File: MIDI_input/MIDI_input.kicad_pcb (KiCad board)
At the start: 2 copper layers, 50 x 40 mm, 21 parts, among them J1 Conn_01x04, U1 6N138

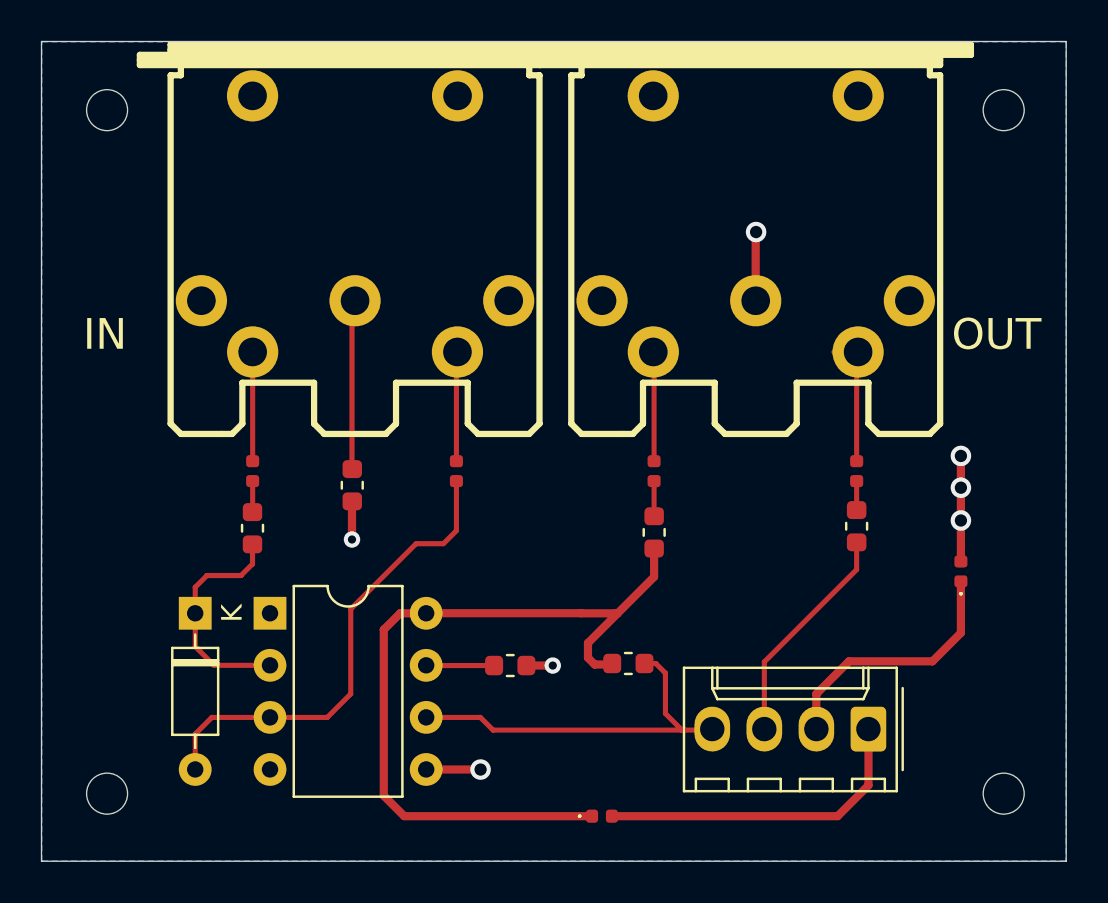
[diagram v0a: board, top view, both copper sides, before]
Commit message: Updates MIDI IO board
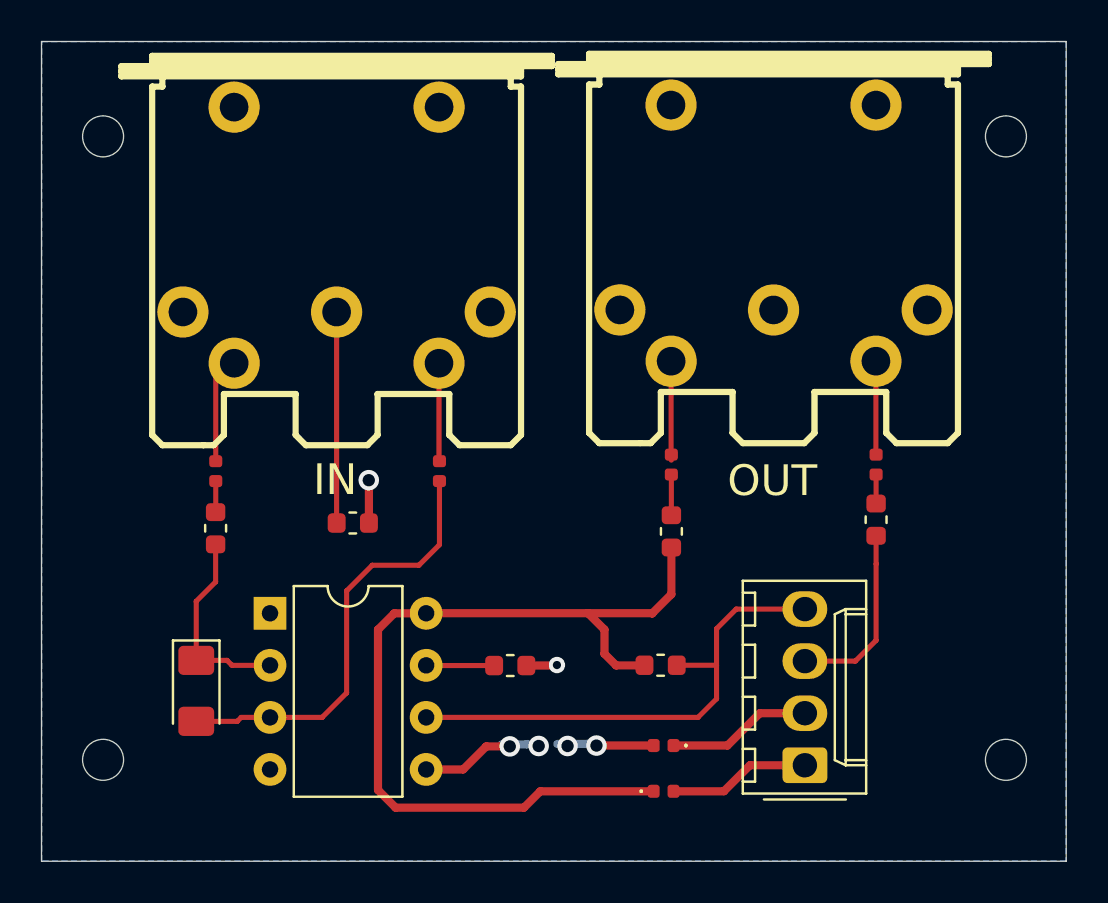
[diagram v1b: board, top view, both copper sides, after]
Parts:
- D1: footprint Diode_THT:D_DO-35_SOD27_P7.62mm_Horizontal -> Diode_SMD:D_1206_3216Metric_Pad1.42x1.75mm_HandSolder
- moved D3 16.8 mm to (44.3, 48.4), turned to 180 degrees
- moved D1 3.79 mm to (21.5, 45.8)
- moved J1 3.57 mm to (51.2, 49.4), turned to 90 degrees
- moved D2 3.24 mm to (44.3, 50.6)
- moved C1 1.84 mm to (29.2, 37.6), turned to 0 degrees
- moved FB3 1.80 mm to (22.5, 35.0)
- moved R3 1.80 mm to (22.5, 37.8)
- moved H2 1.66 mm to (17.0, 49.1)
- moved H4 1.65 mm to (61.0, 49.1)
- moved R4 1.58 mm to (44.2, 44.5)
- moved H1 1.29 mm to (17.0, 18.7)
- moved H3 1.28 mm to (61.0, 18.7)
- moved J_IN_1 1.06 mm to (28.4, 24.3)
- moved FB1 1.00 mm to (54.7, 34.7)
- moved R1 1.00 mm to (54.7, 37.4)
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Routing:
- net Net-(D2-Pad2): track 15.9 -> 6.94 mm
- net RX: track 18.6 -> 24.6 mm
- net +5V: track 37.7 -> 43.4 mm
- net Net-(D3-Pad1): track 12.5 -> 7.06 mm
- net Net-(C1-Pad1): track 8.14 -> 10.3 mm
- net TX: track 11.0 -> 9.00 mm
- net Net-(D1-Pad2): track 23.3 -> 21.5 mm
- net Net-(D1-Pad1): track 11.1 -> 9.75 mm
- net Net-(FB1-Pad1): track 5.41 -> 4.56 mm
- net Net-(FB2-Pad2): track 5.35 -> 4.58 mm
- net Net-(FB4-Pad2): track 5.35 -> 4.79 mm
- net Net-(FB3-Pad2): track 5.33 -> 4.80 mm
- net GND: track 14.2 -> 13.7 mm, vias 7 -> 6
